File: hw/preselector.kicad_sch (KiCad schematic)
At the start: 64 parts, among them U401 74AHC04, U402 74AHC04, U403 MCP23S17_SS, U404 74AHC04, U405 74AHC04, U406 74AHC04, U407 74AHC04, U408 74AHC04, U409 74AHC04, U410 74AHC04, U411 74AHC04, U412 74AHC04, U413 74AHC04, U414 74AHC04, U415 74AHC04

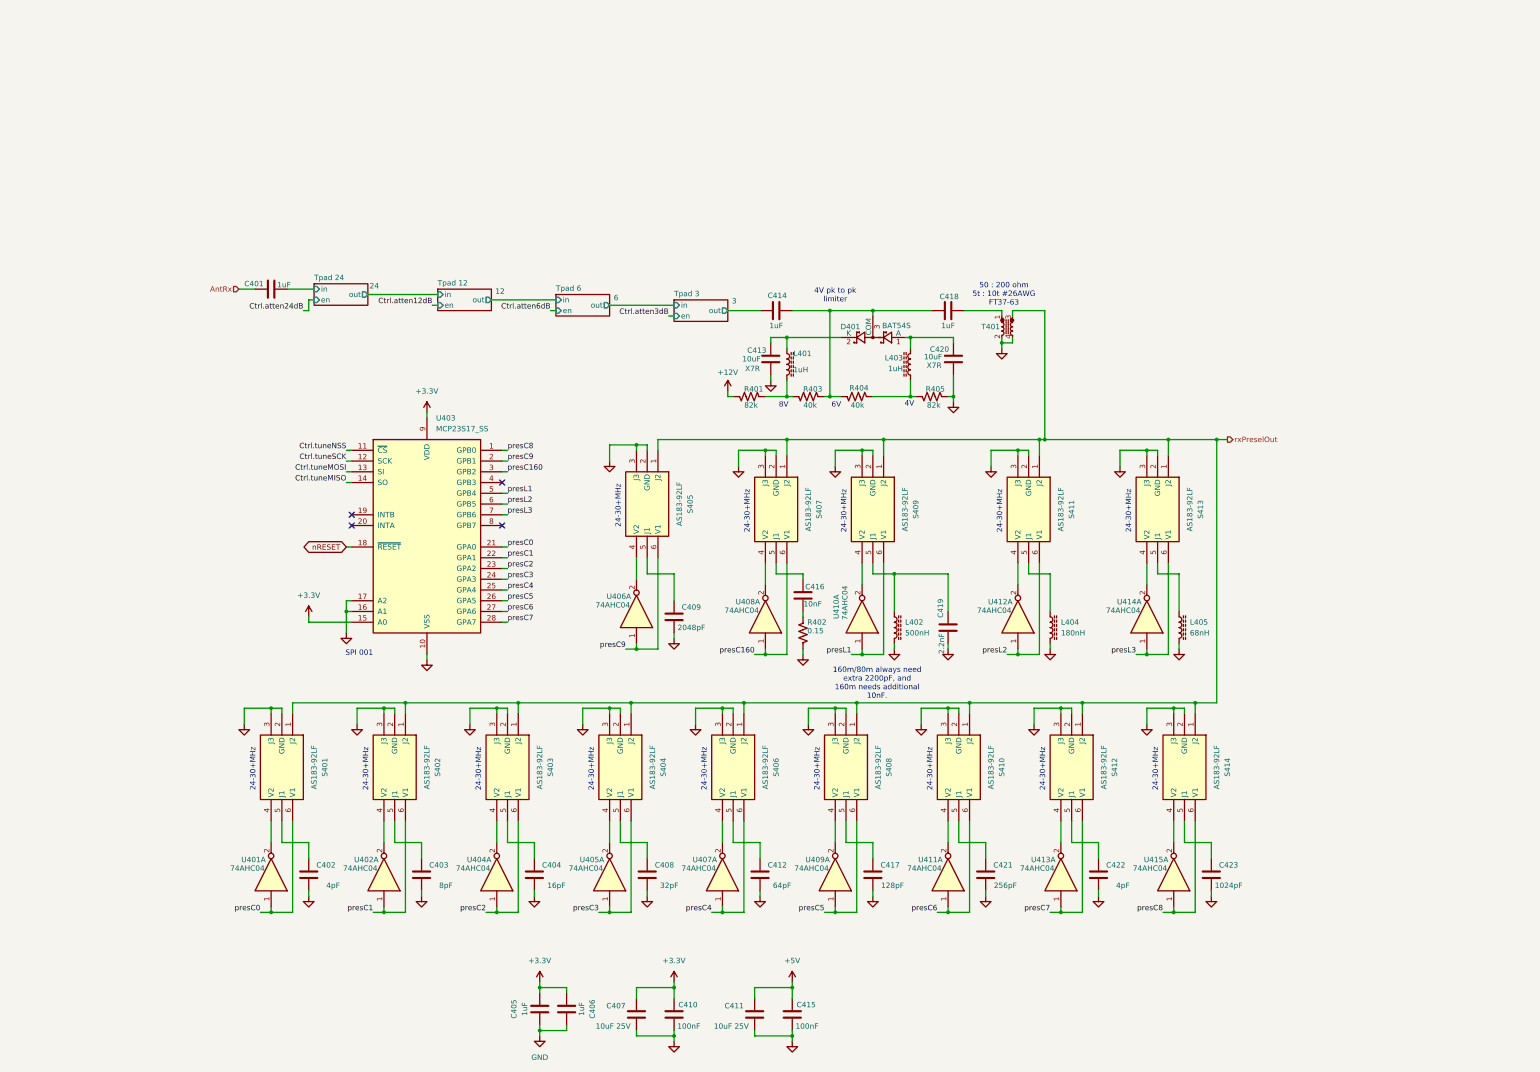
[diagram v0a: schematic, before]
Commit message: QSK rx is now enabled by two series MOSFETs and a third set in series/shunt switch configuration. Rx is now general coverage from 1MHz to 30MHz.
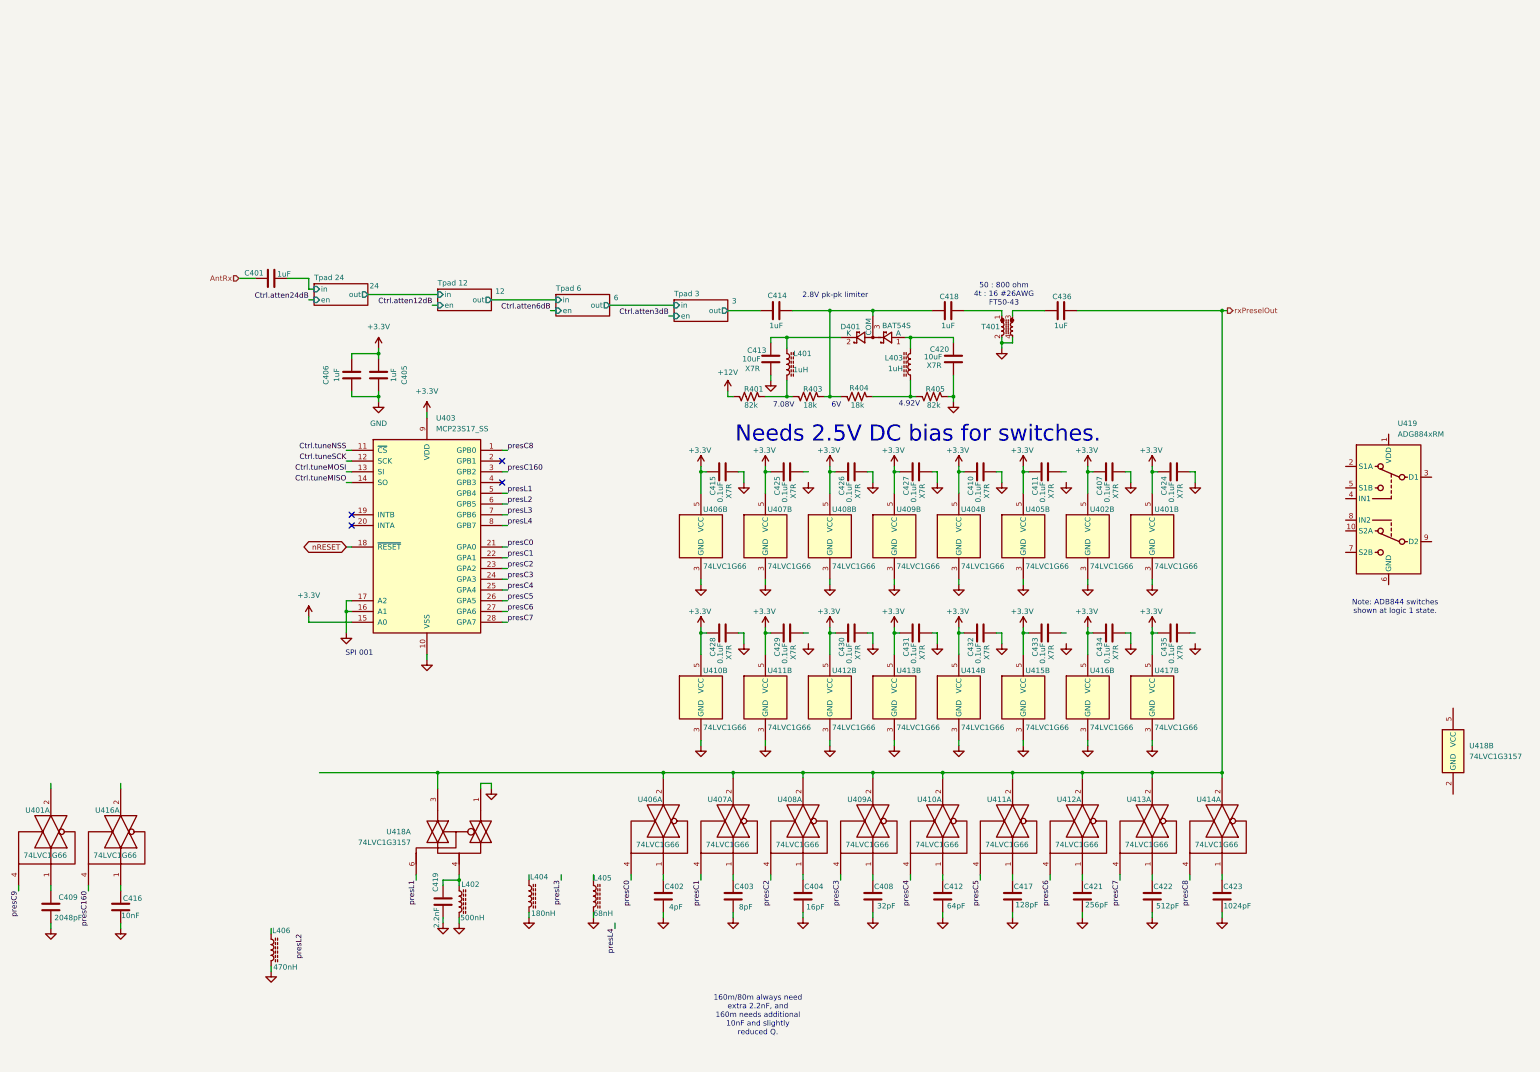
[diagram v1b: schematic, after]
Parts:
- removed R402: 0.15, symbol Device:R_US
- removed S401, S402, S403, S404, S405, S406, S407, S408, S409, S410, S411, S412, S413, S414: AS183-92LF, SOT65P220X110-6N, symbol AS183-92LF:AS183-92LF
- removed U401, U402, U404, U405, U406, U407, U408, U409, U410, U411, U412, U413, U414, U415: 74AHC04, symbol 74xx:74AHC04
- added C424, C425, C426, C427, C428, C429, C430, C431, C432, C433, C434, C435: 0.1uF, symbol Device:C
- added C436: 1uF, symbol Device:C
- added L406: 470nH, symbol Device:L_Ferrite
- added U401, U402, U404, U405, U406, U407, U408, U409, U410, U411, U412, U413, U414, U415, U416, U417: 74LVC1G66, Package_TO_SOT_SMD:SOT-223-5, symbol 74xGxx:74LVC1G66
- added U418: 74LVC1G3157, symbol 74xGxx:74LVC1G3157
- added U419: ADG884xRM, Package_SO:MSOP-10_3x3mm_P0.5mm, symbol Analog_Switch:ADG884xRM
- C407, C411: value 10uF 25V -> 0.1uF; footprint Capacitor_SMD:C_0805_2012Metric -> (none); cap-type (none) -> X7R
- C410, C415: value 100nF -> 0.1uF; footprint Capacitor_SMD:C_0805_2012Metric -> (none); cap-type (none) -> X7R
- C422: value 4pF -> 512pF
- R403, R404: value 40k -> 18k
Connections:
- net +5V is gone; now on net +3.3V: C411.2, C415.2
- net +3.3V: now also C424.2, C425.2, C426.2, C427.2, C428.2, C429.2, C430.2, C431.2, C432.2, C433.2, C434.2, C435.2, U401.5 (VCC), U402.5 (VCC), U404.5 (VCC), U405.5 (VCC), U406.5 (VCC), U407.5 (VCC), U408.5 (VCC), U409.5 (VCC), U410.5 (VCC), U411.5 (VCC), U412.5 (VCC), U413.5 (VCC), U414.5 (VCC), U415.5 (VCC), U416.5 (VCC), U417.5 (VCC)
- net GND: now also C416.2, C424.1, C426.1, C427.1, C428.1, C430.1, C431.1, C432.1, C434.1, L406.2, U401.3 (GND), U402.3 (GND), U404.3 (GND), U405.3 (GND), U406.3 (GND), U407.3 (GND), U408.3 (GND), U409.3 (GND), U410.3 (GND), U411.3 (GND), U412.3 (GND), U413.3 (GND), U414.3 (GND), U415.3 (GND), U416.3 (GND), U417.3 (GND), U418.1; no longer C411.1
- net presC0: now also U406.4
- net presC1: now also U407.4
- net presC160: now also U416.4
- net presC2: now also U408.4
- net presC3: now also U409.4
- net presC4: now also U410.4
- net presC5: now also U411.4
- net presC6: now also U412.4
- net presC7: now also U413.4
- net presC8: now also U414.4
- net presC9: now also U401.4; no longer U403.2 (GPB1)
- net presL1: now also U418.6
- net rxPreselOut: now also C436.1, U406.2, U407.2, U408.2, U409.2, U410.2, U411.2, U412.2, U413.2, U414.2, U418.3; no longer T401.3
- net at C416.1: now also U416.1
- net at C417.1: now also U411.1
- net at C408.1: now also U409.1
- net at C412.1: now also U410.1
- net at C409.1: now also U401.1
- net at C402.1: now also U406.1
- net at C404.1: now also U408.1
- net at C421.1: now also U412.1
- net at C419.1, L402.1: now also U418.4
- net at C403.1: now also U407.1
- net at C423.1: now also U414.1
- net at C422.1: now also U413.1
- net presL4: now reaches U403.8 (GPB7)
- new net: C436.2, T401.3
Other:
- note added: "160m/80m always need extra 2.2nF, and 160m needs additional 10nF and slightly reduced Q."
- note added: "2.8V pk-pk limiter"
- note added: "4.92V"
- note added: "50 : 800 ohm 4t : 16 #26AWG FT50-43"
- note added: "7.08V"
- note added: "Needs 2.5V DC bias for switches."
- note added: "Note: ADB844 switches shown at logic 1 state."
- note removed: "160m/80m always need extra 2200pF, and 160m needs additional 10nF."
- note removed: "24-30+MHz"
- note removed: "4V"
- note removed: "4V pk to pk limiter"
- note removed: "50 : 200 ohm 5t : 10t #26AWG FT37-63"
- note removed: "8V"
- moved on the sheet: C401, C402, C403, C404, C405, C406, C408, C409, C412, C416, C417, C419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

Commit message: Starting to move to 200 ohm share domain with tx and rx with better cheaper faster switching for attenuators and maybe QSK
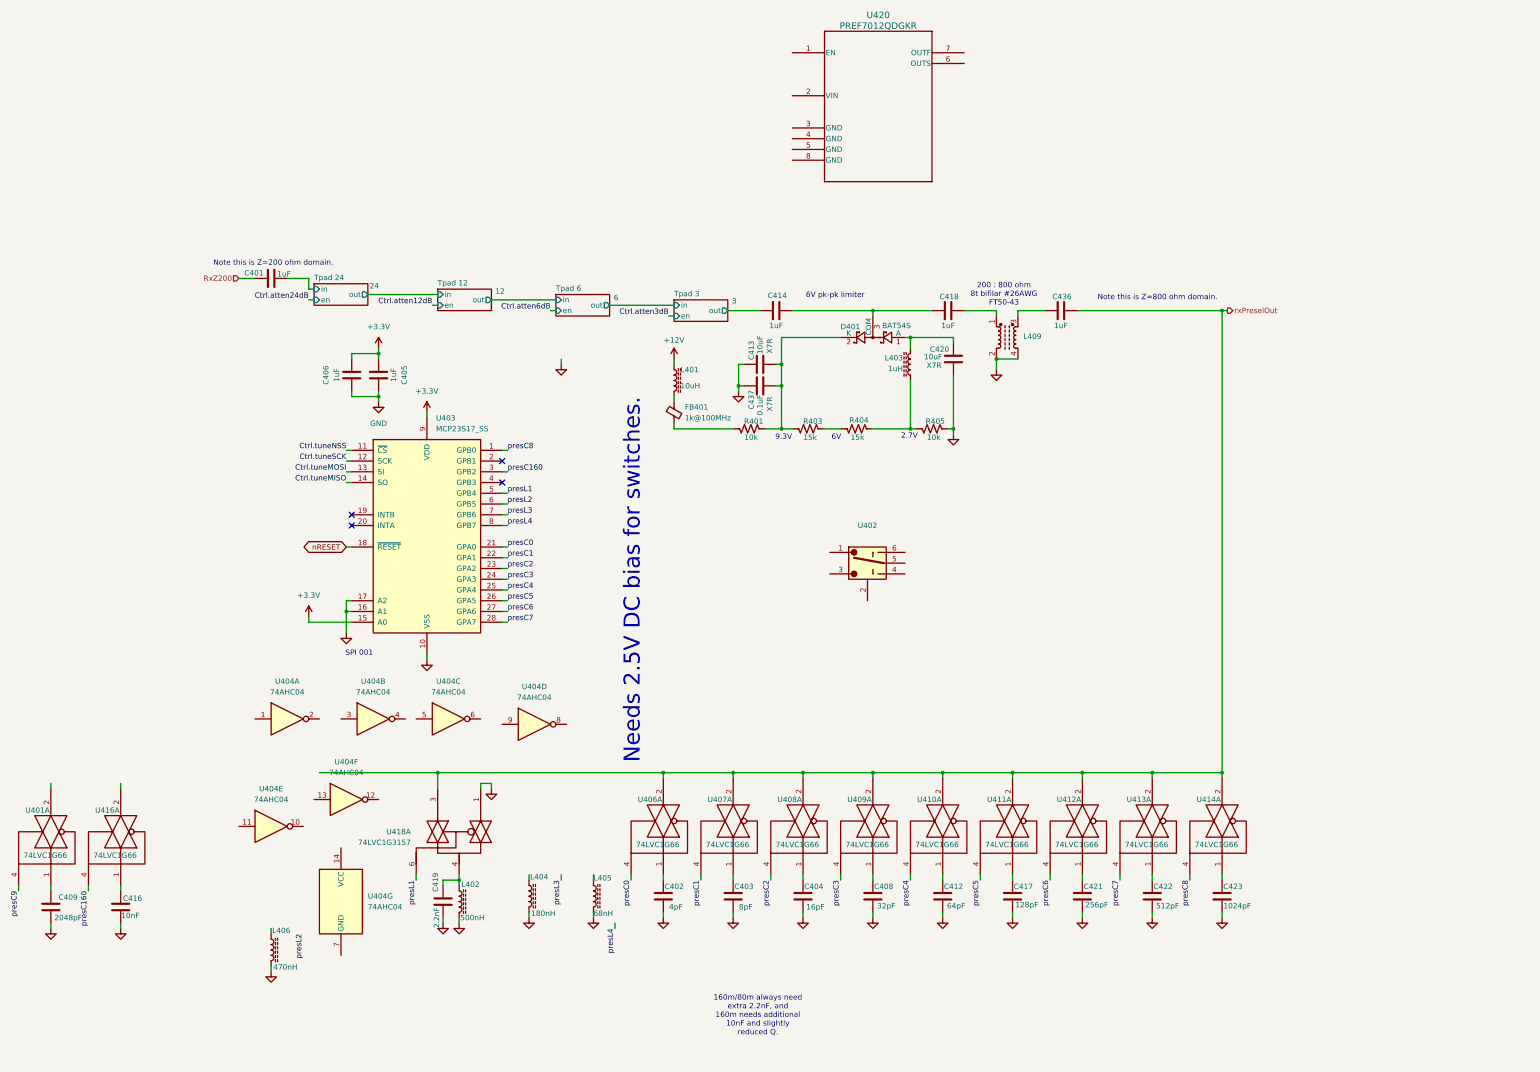
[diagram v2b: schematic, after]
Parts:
- removed C407, C410, C411, C415, C424, C425, C426, C427, C428, C429, C430, C431, C432, C433, C434, C435: 0.1uF, symbol Device:C
- removed T401: ~, symbol Device:L_Ferrite_Coupled_Small
- removed unit 2 of U401
- removed U402, U404, U405, U415, U417: 74LVC1G66, Package_TO_SOT_SMD:SOT-223-5, symbol 74xGxx:74LVC1G66
- removed unit 2 of U406
- removed unit 2 of U407
- removed unit 2 of U408
- removed unit 2 of U409
- removed unit 2 of U410
- removed unit 2 of U411
- removed unit 2 of U412
- removed unit 2 of U413
- removed unit 2 of U414
- removed unit 2 of U416
- removed unit 2 of U418
- removed U419: ADG884xRM, Package_SO:MSOP-10_3x3mm_P0.5mm, symbol Analog_Switch:ADG884xRM
- added C437: 0.1uF, symbol Device:C
- added FB401: 1k@100MHz, symbol Device:FerriteBead_Small
- added L409: 8t bifilar, symbol Device:L_Ferrite_Coupled
- added U402: ~, symbol Library:AS183-92LF
- added U404: 74AHC04, Package_SO:TSSOP-14_4.4x5mm_P0.65mm, symbol 74xx:74AHC04
- added U420: PREF7012QDGKR, VSSOP8_DGK_TEX, symbol PREF7012QDGKR:PREF7012QDGKR
- L401: value 1uH -> 10uH
- R401, R405: value 82k -> 10k
- R403, R404: value 18k -> 15k
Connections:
- net +12V: now also L401.1; no longer R401.1
- net GND: now also C413.2, C437.2, L409.2, L409.4; no longer C413.1
- net at R401.2, R403.1: now also C413.1, D401.2 (K), C437.1; no longer L401.2
- net at C414.1, C418.2, D401.3 (COM): no longer R403.2, R404.1
- net at C418.1: now also L409.1
- net at C436.2: now also L409.3
- net AntRx renamed RxZ200
- new net: R403.2, R404.1
- new net: FB401.1, L401.2
- new net: FB401.2, R401.1
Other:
- note added: "2.7V"
- note added: "200 : 800 ohm 8t bifilar #26AWG FT50-43"
- note added: "6V pk-pk limiter"
- note added: "9.3V"
- note added: "Note this is Z=200 ohm domain."
- note added: "Note this is Z=800 ohm domain."
- note removed: "2.8V pk-pk limiter"
- note removed: "4.92V"
- note removed: "50 : 800 ohm 4t : 16 #26AWG FT50-43"
- note removed: "7.08V"
- note removed: "Note: ADB844 switches shown at logic 1 state."
- moved on the sheet: C413, L401, R401, R403, R404, R405
